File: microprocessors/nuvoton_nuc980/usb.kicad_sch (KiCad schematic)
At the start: 6 parts, among them J2 USB_C (16 + 8), U12 TESD5V0V4UCX6 RFG

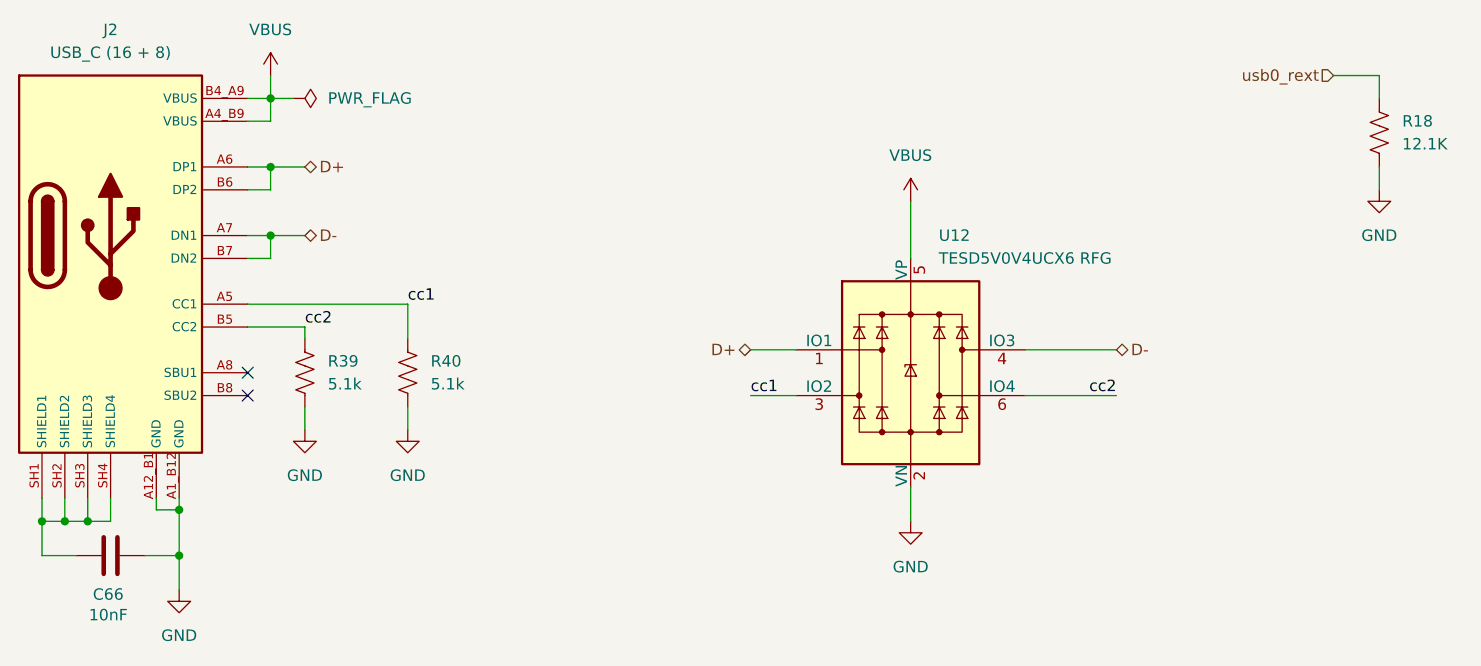
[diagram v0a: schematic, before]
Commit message: feat: cotti leds with new library format
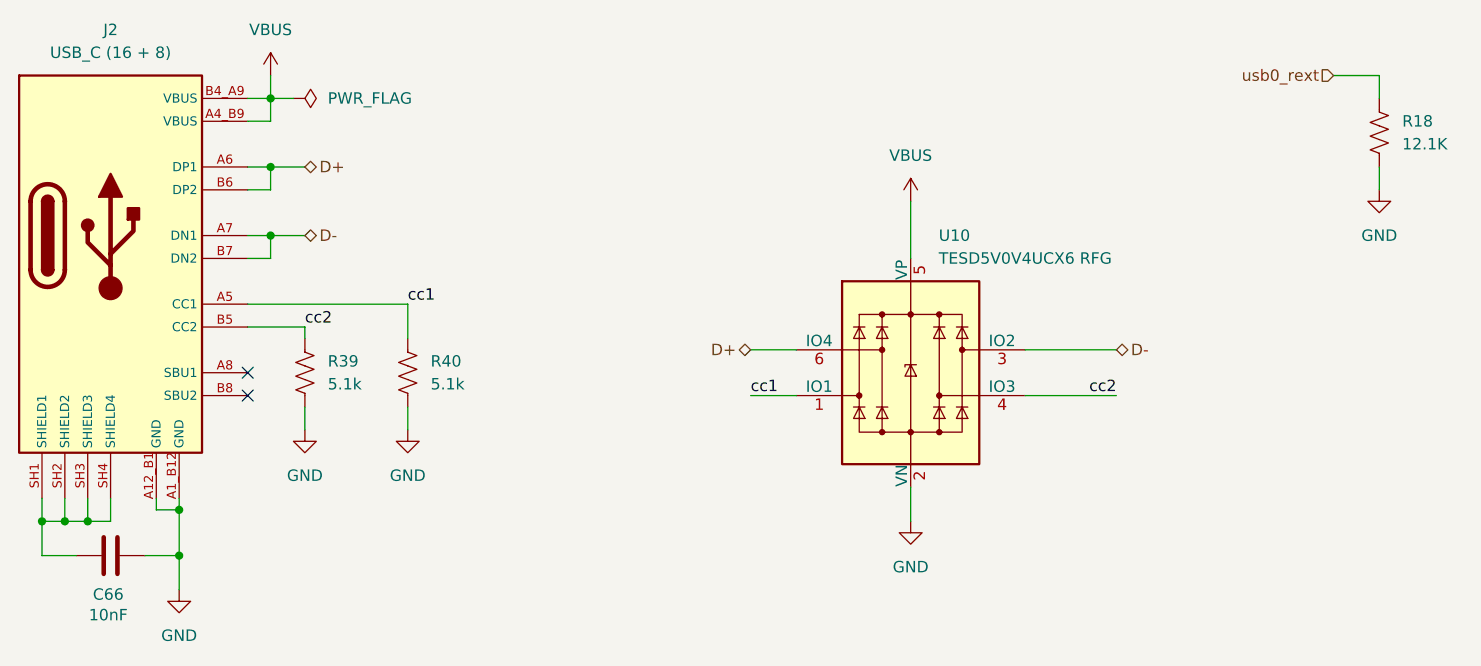
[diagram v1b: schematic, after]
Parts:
- removed J2: USB_C (16 + 8), project_footprints:SAMESKY_UJ20-C-H-G-SMT-5-P16-TR, symbol project_symbols:USB_C
- removed U12: TESD5V0V4UCX6 RFG, Package_TO_SOT_SMD:SOT-23-6, symbol Power_Protection:CDSOT236-0504C
- added J2: USB_C (16 + 8), cotti_footprints:SAMESKY_UJ20-C-H-G-SMT-5-P16-TR, symbol cotti_usb:USB_C_16+8
- added U10: TESD5V0V4UCX6 RFG, Package_TO_SOT_SMD:SOT-23-6, symbol cotti_usb:TVS_5V
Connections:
- net D+: now also J2.A6 (DP1), J2.B6 (DP2), U10.6 (IO4)
- net D-: now also J2.A7 (DN1), J2.B7 (DN2), U10.3 (IO2)
- net GND: now also J2.A12_B1 (GND), J2.A1_B12 (GND), U10.2 (VN)
- net VBUS: now also J2.A4_B9 (VBUS), J2.B4_A9 (VBUS), U10.5 (VP)
- net cc1: now also J2.A5 (CC1), U10.1 (IO1)
- net cc2: now also J2.B5 (CC2), U10.4 (IO3)
- net at C66.1: now also J2.SH1 (SHIELD1), J2.SH2 (SHIELD2), J2.SH3 (SHIELD3), J2.SH4 (SHIELD4)
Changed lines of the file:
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@@
+	)
+	(symbol
+		(lib_id "cotti_usb:USB_C_16+8")
+		(at 83.82 48.26 0)
+		(unit 1)
+		(exclude_from_sim no)
+		(in_bom yes)
+		(on_board yes)
+		(dnp no)
+		(fields_autoplaced yes)
+		(property "Reference" "J2"
+			(at 93.98 43.18 0)
+			(effects
+				(font
+					(size 1.27 1.27)
+				)
+			)
+		)
+		(property "Value" "USB_C (16 + 8)"
+			(at 93.98 45.72 0)
+			(effects
+				(font
+					(size 1.27 1.27)
+				)
+			)
+		)
+		(property "Footprint" "cotti_footprints:SAMESKY_UJ20-C-H-G-SMT-5-P16-TR"
+			(at 84.836 26.416 0)
+			(effects
+				(font
+					(size 1.27 1.27)
+				)
+				(hide yes)
+			)
+		)
+		(property "Datasheet" "https://www.sameskydevices.com/product/resource/uj20-c-h-g-smt-5-p16-tr.pdf"
+			(at 87.122 30.226 0)
+			(effects
+				(font
+					(size 1.27 1.27)
+				)
+				(hide yes)
+			)
+		)
+		(property "Description" "USB-C (USB TYPE-C) USB 2.0 Receptacle Connector 24 (16+8 Dummy) Position Surface Mount, Right Angle; Through Hole"
+			(at 85.852 34.29 0)
+			(effects
+				(font
+					(size 1.27 1.27)
+				)
+				(hide yes)
+			)
+		)
+		(property "Digikey" "https://www.digikey.com/en/products/detail/same-sky-formerly-cui-devices/UJ20-C-H-G-SMT-5-P16-TR/24818593"
+			(at 93.218 39.878 0)
+			(effects
+				(font
+					(size 1.27 1.27)
+				)
+				(hide yes)
+			)
+		)
+		(property "Mfr." "Same Sky (Formerly CUI Devices)"
+			(at 84.582 22.606 0)
+			(effects
+				(font
+					(size 1.27 1.27)
+				)
+				(hide yes)
+			)
+		)
+		(property "Mfr. P/N" "UJ20-C-H-G-SMT-5-P16-TR"
+			(at 85.852 37.338 0)
+			(effects
+				(font
+					(size 1.27 1.27)
+				)
+				(hide yes)
+			)
+		)
+		(pin "B8"
+		)
+		(pin "B6"
+		)
+		(pin "SH1"
+		)
+		(pin "B7"
+		)
+		(pin "A6"
+		)
+		(pin "B4_A9"
+		)
+		(pin "A12_B1"
+		)
+		(pin "A8"
+		)
+		(pin "A7"
+		)
+		(pin "SH2"
+		)
+		(pin "SH3"
+		)
+		(pin "SH4"
+		)
+		(pin "A4_B9"
+		)
+		(pin "A1_B12"
+		)
+		(pin "A5"
+		)
+		(pin "B5"
+		)
+		(instances
+			(project ""
+				(path "/109442c7-6d61-4448-a955-a6cd87e17c77/fd687155-536a-49ae-b1a5-a1fbc23322ab"
+					(reference "J2")
+					(unit 1)
+				)
+			)
+		)
 	)
 	(symbol
@@
 	)
 	(symbol
-		(lib_id "Power_Protection:CDSOT236-0504C")
+		(lib_id "cotti_usb:TVS_5V")
 		(at 182.88 81.28 0)
 		(unit 1)
@@
 		(dnp no)
 		(fields_autoplaced yes)
-		(property "Reference" "U12"
+		(property "Reference" "U10"
 			(at 185.9981 66.04 0)
 			(effects
@@
 		)
 		(property "Footprint" "Package_TO_SOT_SMD:SOT-23-6"
-			(at 200.66 92.71 0)
+			(at 181.356 55.372 0)
 			(effects
 				(font
@@
 		)
 		(property "Datasheet" "https://services.taiwansemi.com/storage/resources/datasheet/TESD5V0V4UCX6_B2003.pdf"
-			(at 182.88 81.28 0)
+			(at 181.864 51.816 0)
 			(effects
 				(font
@@
 		)
 		(property "Description" "15V Clamp 5A (8/20µs) Ipp Tvs Diode Surface Mount SOT-26"
-			(at 182.88 81.28 0)
+			(at 187.96 44.196 0)
 			(effects
 				(font
@@
 		)
 		(property "Digikey" "https://www.digikey.com/en/products/detail/taiwan-semiconductor-corporation/TESD5V0V4UCX6-RFG/7623393"
-			(at 182.88 81.28 0)
+			(at 186.69 47.752 0)
 			(effects
 				(font
@@
 		)
 		(property "Mfr." "Taiwan Semiconductor Corporation"
-			(at 182.88 81.28 0)
+			(at 183.388 41.148 0)
 			(effects
 				(font
@@
 		)
 		(property "Mfr. P/N" "TESD5V0V4UCX6 RFG"
-			(at 182.88 81.28 0)
-			(effects
-				(font
-					(size 1.27 1.27)
-				)
-				(hide yes)
-			)
+			(at 182.88 37.084 0)
+			(effects
+				(font
+					(size 1.27 1.27)
+				)
+				(hide yes)
+			)
+		)
+		(pin "3"
+		)
+		(pin "2"
 		)
 		(pin "4"
 		)
-		(pin "1"
-		)
-		(pin "3"
-		)
 		(pin "5"
 		)
 		(pin "6"
 		)
-		(pin "2"
+		(pin "1"
 		)
 		(instances
 			(project ""
 				(path "/109442c7-6d61-4448-a955-a6cd87e17c77/fd687155-536a-49ae-b1a5-a1fbc23322ab"
-					(reference "U12")
+					(reference "U10")
 					(unit 1)
 				)
@@
 					(unit 1)
 				)
-			)
-		)
-	)
-	(symbol
-		(lib_id "project_symbols:USB_C")
-		(at 83.82 48.26 0)
-		(unit 1)
-		(exclude_from_sim no)
-		(in_bom yes)
-		(on_board yes)
-		(dnp no)
-		(fields_autoplaced yes)
-		(property "Reference" "J2"
-			(at 93.98 43.18 0)
-			(effects
-				(font
-					(size 1.27 1.27)
-				)
-			)
-		)
-		(property "Value" "USB_C (16 + 8)"
-			(at 93.98 45.72 0)
-			(effects
-				(font
-					(size 1.27 1.27)
-				)
-			)
-		)
-		(property "Footprint" "project_footprints:SAMESKY_UJ20-C-H-G-SMT-5-P16-TR"
-			(at 84.836 26.416 0)
-			(effects
-				(font
-					(size 1.27 1.27)
-				)
-				(hide yes)
-			)
-		)
-		(property "Datasheet" "https://www.sameskydevices.com/product/resource/uj20-c-h-g-smt-5-p16-tr.pdf"
-			(at 87.122 30.226 0)
-			(effects
-				(font
-					(size 1.27 1.27)
-				)
-				(hide yes)
-			)
-		)
-		(property "Description" "USB-C (USB TYPE-C) USB 2.0 Receptacle Connector 24 (16+8 Dummy) Position Surface Mount, Right Angle; Through Hole"
-			(at 85.852 34.29 0)
-			(effects
-				(font
-					(size 1.27 1.27)
-				)
-				(hide yes)
-			)
-		)
-		(property "Digikey" "https://www.digikey.com/en/products/detail/same-sky-formerly-cui-devices/UJ20-C-H-G-SMT-5-P16-TR/24818593"
-			(at 93.218 39.878 0)
-			(effects
-				(font
-					(size 1.27 1.27)
-				)
-				(hide yes)
-			)
-		)
-		(property "Mfr." "Same Sky (Formerly CUI Devices)"
-			(at 84.582 22.606 0)
-			(effects
-				(font
-					(size 1.27 1.27)
-				)
-				(hide yes)
-			)
-		)
-		(property "Mfr. P/N" "UJ20-C-H-G-SMT-5-P16-TR"
-			(at 85.852 37.338 0)
-			(effects
-				(font
-					(size 1.27 1.27)
-				)
-				(hide yes)
-			)
-		)
-		(pin "A7"
-		)
-		(pin "B5"
-		)
-		(pin "A6"
-		)
-		(pin "B6"
-		)
-		(pin "A1_B12"
-		)
-		(pin "A4_B9"
-		)
-		(pin "B7"
-		)
-		(pin "SH1"
-		)
-		(pin "A12_B1"
-		)
-		(pin "B8"
-		)
-		(pin "SH2"
-		)
-		(pin "SH3"
-		)
-		(pin "SH4"
-		)
-		(pin "B4_A9"
-		)
-		(pin "A8"
-		)
-		(pin "A5"
-		)
-		(instances
-			(project ""
-				(path "/109442c7-6d61-4448-a955-a6cd87e17c77/fd687155-536a-49ae-b1a5-a1fbc23322ab"
-					(reference "J2")
-					(unit 1)
-				)

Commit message: feat: ERC passing cotti-nuvoton
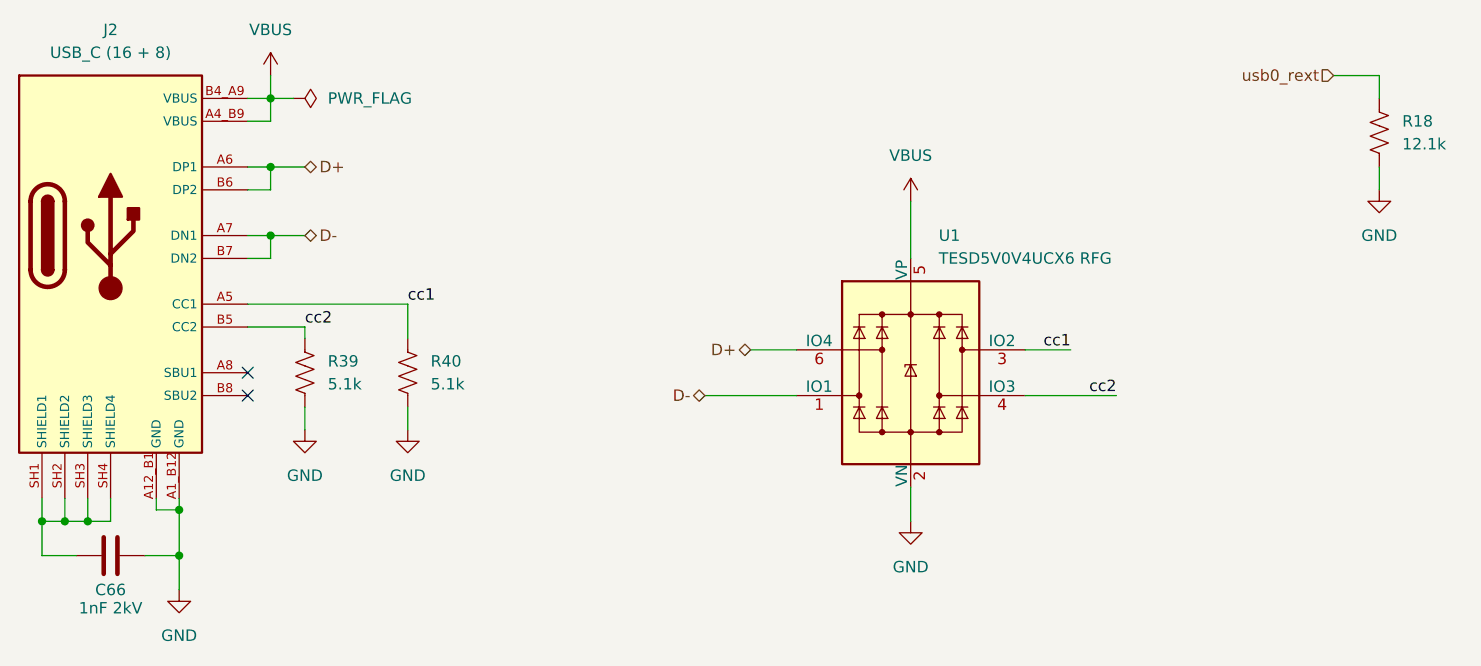
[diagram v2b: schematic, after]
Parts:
- removed U10: TESD5V0V4UCX6 RFG, Package_TO_SOT_SMD:SOT-23-6, symbol cotti_usb:TVS_5V
- added U1: TESD5V0V4UCX6 RFG, Package_TO_SOT_SMD:SOT-23-6, symbol cotti_usb:IC_TVS_5V
- C66: value 10nF -> 1nF 2kV; footprint (none) -> Capacitor_SMD:C_1206_3216Metric_Pad1.33x1.80mm_HandSolder; Digikey (none) -> https://www.digikey.com/en/products/detail/walsin-technolog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; Mfr. (none) -> Walsin Technology Corporation; Mfr. P/N (none) -> 1206B102M202CT
- R18: value 12.1K -> 12.1k; footprint (none) -> Resistor_SMD:R_0805_2012Metric_Pad1.20x1.40mm_HandSolder; Digikey (none) -> https://www.digikey.com/en/products/detail/yageo/AC0805FR-0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; Mfr. (none) -> YAGEO; Mfr. P/N (none) -> AC0805FR-0712K1L
- R39, R40: footprint (none) -> Resistor_SMD:R_0805_2012Metric_Pad1.20x1.40mm_HandSolder; Digikey (none) -> https://www.digikey.com/en/products/detail/yageo/RC0805FR-1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; Mfr. (none) -> YAGEO; Mfr. P/N (none) -> RC0805FR-135K1L
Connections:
- net D+: now also U1.6 (IO4)
- net D-: now also U1.1 (IO1)
- net GND: now also U1.2 (VN)
- net VBUS: now also U1.5 (VP)
- net cc1: now also U1.3 (IO2)
- net cc2: now also U1.4 (IO3)
